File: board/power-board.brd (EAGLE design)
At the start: 95.9 x 90.2 mm, 366 parts, among them J1 H1, J2 H2, J6 DF13-8P-1.25DS, J7 DF13-10P-1.25DS, J8 DF13-4P-1.25DS, J9 DF13-4P-1.25DS, Q1 TPC8120, Q2 TPC8120, Q3 SI7288, U1 INA214DCK, U10 INA214DCK, U11 INA214DCK, U12 INA214DCK, U13 MCP6561T-E/LT, U14 INA214DCK, U15 SN74AUP1G00DCK, U16 SN74LVC1G373DCK, U17 NTHD4508NT1, U18 MCP6561T-E/LT, U19 INA214DCK, U2 INA214DCK, U20 SN74AUP1G00DCK, U21 SN74LVC1G373DCK, U22 NTHD4508NT1, U23 MCP6561T-E/LT, U24 INA214DCK, U25 SN74AUP1G00DCK, U26 SN74LVC1G373DCK, U27 NTHD4508NT1, U28 MCP6561T-E/LT, U29 INA214DCK, U3 INA214DCK, U30 SN74AUP1G00DCK, U31 SN74LVC1G373DCK, U32 NTHD4508NT1, U33 MCP6561T-E/LT, U34 INA214DCK, U35 SN74AUP1G00DCK, U36 SN74LVC1G373DCK, U37 NTHD4508NT1, U38 MCP6561T-E/LT, U39 INA214DCK, U4 INA214DCK, U40 SN74AUP1T08DCK, U41 SN74LVC1G373DCK, U42 FDS8858CZ, U43 TLV3491AIDBV, U44 TPS62132RGT, U45 FDS8858CZ, U46 TLV3491AIDBV, U47 TPS62133RGT, U48 FDS8858CZ, U49 MSP430F2132, U5 INA214DCK, U50 ADG732, U51 SPV1040T, U52 SPV1040T, U53 BQ24650_RVA_16, U54 INA214DCK, U6 INA214DCK, U7 INA214DCK, U8 INA214DCK, U9 INA214DCK, X1 32.768k

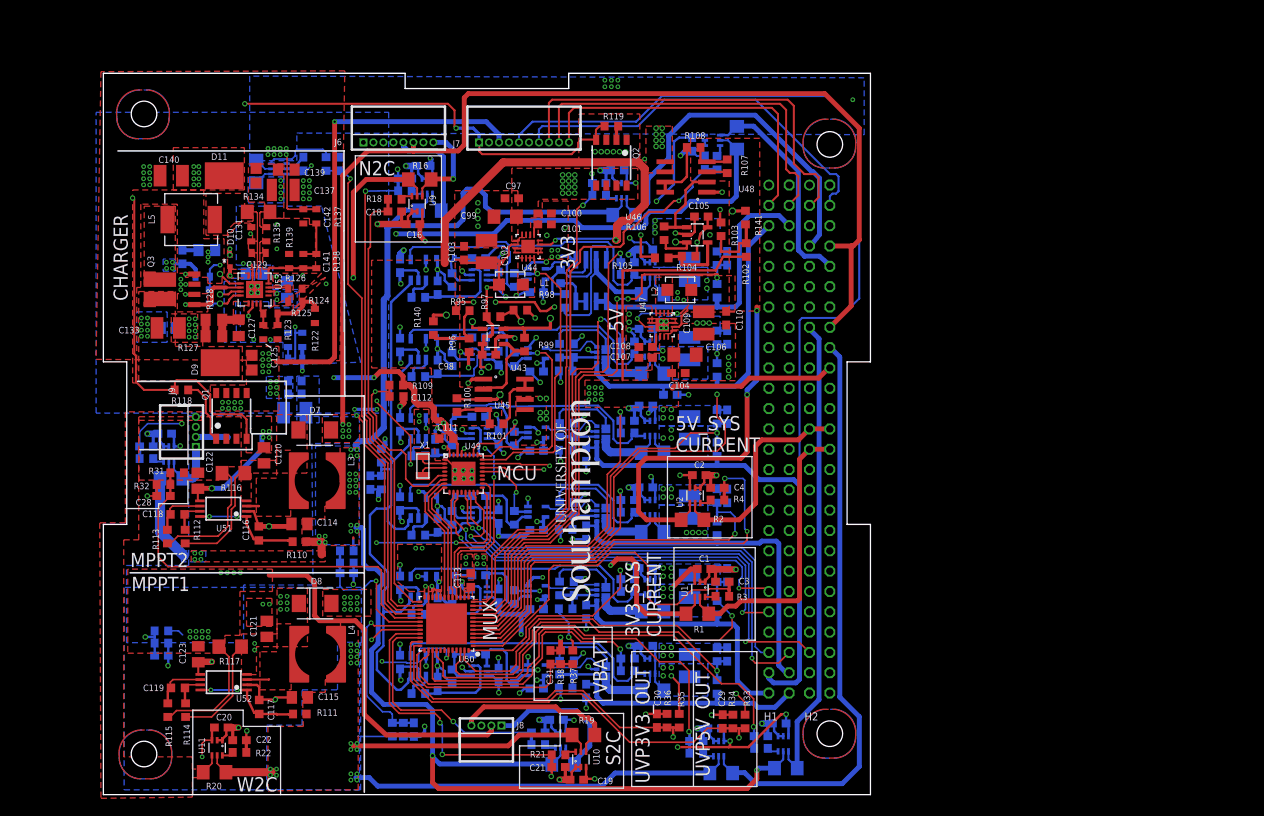
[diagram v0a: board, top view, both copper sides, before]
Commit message: removing deployment switches, adding testpoints
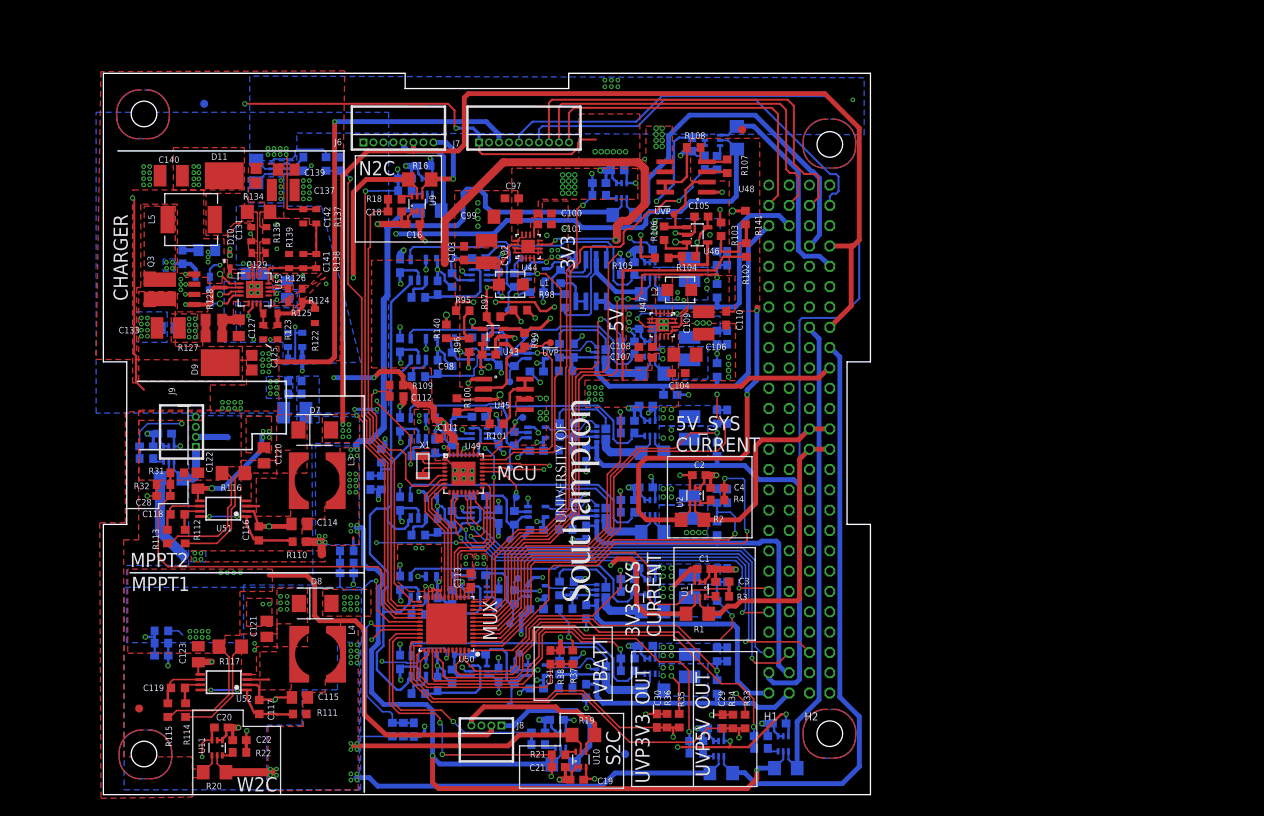
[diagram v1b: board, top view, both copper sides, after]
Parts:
- removed Q1, Q2: TPC8120, gdp_pss_library:SOP8
- removed R118, R119: 1Meg, rcl:R0603
- added FID1, FID2, FID3, FID4: FIDUCIAL1X2-STOP, fiducial:FIDUCIAL-1X2-STOP
- added TP1, TP10, TP11, TP12, TP13, TP14, TP2, TP3, TP4, TP5, TP6, TP7, TP8, TP9: PTR1TP09R, testpad:TP09R
- R39: value 442m -> 50m
- R48: value 43m -> 124m
- moved R140 1.68 mm to (42.9, 57.9)
- moved R99 0.61 mm to (52.6, 56.9)
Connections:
- net 3V3_BU_RADIO renamed 5V_TX_RADIO
- removed net MPPT_BUS: C122.1, Q1.1, Q1.2, Q1.3, R113.1, R116.1, R118.2, R31.2
- removed net REG_VIN: C100.1, C104.1, C106.1, C107.1, C95.1, C97.1, C99.1, J2.20, Q2.5, Q2.6, Q2.7, Q2.8, R102.1, R37.2, R44.2, R53.2, R62.2, R71.2, R80.2, R84.1, R95.1, U39.4, U44.10, U44.11, U44.12, U44.13, U47.10, U47.11, U47.12, U47.13
- new net 5V_RX_RADIO: C53.1, R55.2, U22.1
- net 3V3_RADIO: no longer C53.1, R55.2, U22.1
- net CHARGE_IN: now also C122.1, R113.1, R116.1, R31.2; no longer Q1.5, Q1.6, Q1.7, Q1.8
- net OCP1_COMP_OUT: now also TP12.TP
- net OCP1_MCU_EN: now also TP11.TP
- net OCP1_SENSEM: now also R44.2
- net OCP2_COMP_OUT: now also TP10.TP
- net OCP2_MCU_EN: now also TP9.TP
- net OCP2_SENSEM: now also R53.2
- net OCP3_COMP_OUT: now also TP8.TP
- net OCP3_MCU_EN: now also TP7.TP
- net OCP3_SENSEM: now also R62.2
- net OCP4_COMP_OUT: now also TP6.TP
- net OCP4_MCU_EN: now also TP5.TP
- net OCP4_SENSEM: now also R71.2
- net OCP5_COMP_OUT: now also TP4.TP
- net OCP5_MCU_EN: now also TP3.TP
- net OCP5_SENSEM: now also R80.2
- net OCP6_COMP_OUT: now also TP2.TP
- net OCP6_MCU_EN: now also TP1.TP
- net RBF_A: no longer Q1.4, Q2.4, R118.1, R119.1
- net UVP3V3_GATE: now also TP13.TP
- net UVP3V3_OUT: no longer R39.1, R48.1, U14.4, U19.4
- net UVP5V_GATE: now also TP14.TP
- net UVP5V_OUT: now also R39.1, R48.1, U14.4, U19.4
- net VBATT: now also C100.1, C104.1, C106.1, C107.1, C95.1, C97.1, C99.1, J2.20, R102.1, R37.2, R84.1, R95.1, U39.4, U44.10, U44.11, U44.12, U44.13, U47.10, U47.11, U47.12, U47.13; no longer Q2.1, Q2.2, Q2.3, R119.2
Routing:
- net REG_VIN: track 79.6 -> 0.00 mm, vias 32 -> 0
- net VBATT: track 14.6 -> 86.2 mm, vias 21 -> 49
- net MPPT_BUS: track 24.4 -> 0.00 mm
- net RBF_A: track 121.9 -> 99.8 mm
- net CHARGE_IN: track 65.3 -> 81.5 mm
- net UVP3V3_OUT: track 344.3 -> 337.7 mm
- net GND: track 311.5 -> 305.3 mm
- net UVP3V3_GATE: track 10.9 -> 15.2 mm
- net N$49: track 25.7 -> 22.5 mm
- net OCP6_COMP_OUT: track 14.5 -> 17.8 mm
- net OCP4_COMP_OUT: track 13.5 -> 16.5 mm
- net OCP1_COMP_OUT: track 12.6 -> 15.5 mm
- net OCP2_COMP_OUT: track 10.6 -> 13.3 mm
- net OCP5_MCU_EN: track 26.0 -> 28.6 mm
- net UVP5V_OUT: track 5.67 -> 8.22 mm
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- removed copper zone on layer 1, net MPPT_BUS
- removed copper zone on layer 1, net REG_VIN
- removed copper zone on layer 16, net REG_VIN
- removed copper zone on layer 2, net REG_VIN
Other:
- board text added: "!UVP"
- board text added: "EN"
- board text added: "OCP"

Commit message: done (hopefully)
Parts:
- added TP15, TP16, TP17, TP18, TP19, TP20, TP21, TP22, TP23, TP24, TP25, TP26, TP27, TP28, TP29, TP30: PTR1TP09R, testpad:TP09R
- moved R141 2.01 mm to (78.8, 70.7)
- moved R102 1.55 mm to (78.9, 67.5)
- moved C29 1.22 mm to (76.2, 9.14)
- moved R27 0.81 mm to (35.3, 8.13)
- moved R4 0.73 mm to (77.4, 36.4)
- moved C30 0.61 mm to (68.6, 9.25)
- moved C4 0.61 mm to (77.4, 38.4)
- moved C85 0.61 mm to (78.6, 57.1)
- moved R100 0.61 mm to (44.8, 48.7)
- moved R2 0.61 mm to (74.2, 34.4)
- moved R25 0.61 mm to (30.4, 31.1)
- moved R34 0.61 mm to (78.1, 9.14)
- moved R37 0.61 mm to (59.3, 17.2)
- moved R47 0.61 mm to (76.1, 17.5)
- moved R56 0.61 mm to (76.1, 27.4)
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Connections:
- removed net 3V3_RADIO: J1.51
- net 3V3_FLIGHT_MCU: now also TP24.TP
- net 3V3_SYS: now also TP16.TP
- net 5V_CAMERA: now also TP25.TP
- net 5V_RX_RADIO: now also J1.51, TP26.TP
- net 5V_SYS: now also TP15.TP
- net 5V_TX_RADIO: now also TP27.TP
- net CHARGE_IN: now also TP28.TP
- net GND: now also TP30.TP
- net MPPT2_OUT: now also TP29.TP
- net OCP1_SENSEM: no longer R44.2
- net OCP2_SENSEM: no longer R53.2
- net OCP3_SENSEM: no longer R62.2
- net OCP4_SENSEM: no longer R71.2
- net OCP5_SENSEM: no longer R80.2
- net OEM615_3V3: now also TP23.TP
- net OEM615_LNA_PWR: now also TP22.TP
- net REG3V3: now also TP21.TP
- net REG5V: now also TP20.TP
- net UVP3V3_OUT: now also TP17.TP; no longer C40.1, C51.1
- net UVP5V_OUT: now also C40.1, C51.1, TP18.TP
- net VBATT: now also R44.2, R53.2, R62.2, R71.2, R80.2, TP19.TP
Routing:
- net RBF_A: track 99.8 -> 0.00 mm, vias 3 -> 0
- net 5V_RX_RADIO: track 0.00 -> 35.8 mm
- net 3V3_RADIO: track 33.1 -> 0.00 mm
- net GND: track 305.3 -> 317.1 mm, vias 198 -> 203
- net REG3V3: track 176.0 -> 165.2 mm, vias 8 -> 6
- net UVP3V3_OUT: track 337.7 -> 348.2 mm, vias 69 -> 64
- net CHARGE_IN: track 81.5 -> 89.8 mm, vias 24 -> 26
- net VBATT: track 86.2 -> 94.3 mm, vias 49 -> 45
- net 3V3_SYS: track 36.4 -> 43.4 mm
- net UVP5V_OUT: track 8.22 -> 15.1 mm, vias 15 -> 23
- net N$6: track 8.67 -> 3.18 mm
- net SYS_5V_CSENSE_MUX: track 55.9 -> 51.9 mm
- net 5V_CAMERA: track 44.6 -> 48.3 mm
- net 5V_TX_RADIO: track 30.0 -> 33.8 mm
- net MPPT1_PV_P: track 199.4 -> 195.7 mm
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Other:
- board text added: "!OCP"
- board text added: "0V"
- board text added: "3V3_SYS"
- board text added: "5V_SYS"
- board text added: "CAM"
- board text added: "CHG IN"
- board text added: "GPS"
- board text added: "LNA"
- board text added: "RX"
- board text added: "Rev 1.1 Mar'17"
- board text added: "S/N"
- board text added: "TX"
- board text added: "UVP 3V3"
- board text added: "UVP 5V"
- board text removed: "H1"
- board text removed: "H2"
- board text removed: "OCP"
- board text removed: "Rev 1.1 Dec'16"
- board text removed: "UVP3V3_OUT"
- board text removed: "UVP5V_OUT"

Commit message: committing WIP
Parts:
- added C143, C148, C153, C158: 1u, rcl:C0603K
- added C144, C149, C154, C159: 100n, rcl:C0603K
- added C145, C146, C150, C151, C155, C156, C160, C161: 10u, rcl:C0805K
- added C147, C152, C157, C162: 4.7u, rcl:C0805K
- added D12, D13, D14, D15: 5V1, diode:SMBJ
- added L6, L7, L8, L9: 10uH, gdp_pss_library:MSS7341
- added R118, R119, R143, R144, R145, R147, R148, R149, R151, R152, R153, R155: 1k, rcl:R0603
- added R142, R146, R150, R154: 10m, rcl:R1206
- added TP31, TP32, TP33, TP34, TP35, TP36: PTR1TP09R, testpad:TP09R
- added U55, U56, U57, U58: SPV1040T, gdp_pss_library:TSSOP8
- moved C28 100.9 mm to (108.3, 32.1)
- moved R31 100.9 mm to (110.0, 35.0)
- moved R32 100.9 mm to (108.3, 33.5)
- moved C20 95.6 mm to (101.1, 49.4)
- moved C22 95.6 mm to (103.4, 47.9)
- moved R20 95.6 mm to (100.3, 43.9)
- moved R22 95.6 mm to (103.4, 46.3)
- moved U11 95.6 mm to (100.6, 46.9)
- moved TP29 93.9 mm to (107.3, 25.0)
- moved TP28 93.1 mm to (104.0, 22.1)
- moved TP30 91.7 mm to (107.5, 23.0)
- moved R111 42.2 mm to (14.1, 51.0), turned to 90 degrees
- moved C117 40.2 mm to (16.1, 51.0), turned to 270 degrees
- moved C115 39.7 mm to (22.1, 51.8)
- moved R115 39.7 mm to (11.0, 50.1), turned to 180 degrees
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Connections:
- net MPPT2_OUT renamed MPPT1_MID
- new net MPPT1H_PV_P: C114.1, L3.1, R110.1
- new net MPPT1L_PV_P: C115.1, L4.1, R111.1
- new net MPPT2H_PV_P: C146.1, L6.1, R143.1
- new net MPPT2L_PV_P: C151.1, L7.1, R147.1
- new net MPPT2_MID: C144.2, C145.2, C146.2, C147.2, C150.1, D12.A, R145.1, R146.1, TP32.TP, U55.2, U55.5
- new net MPPT3H_PV_P: C156.1, L8.1, R151.1
- new net MPPT3L_PV_P: C161.1, L9.1, R155.1
- new net MPPT3_MID: C154.2, C155.2, C156.2, C157.2, C160.1, D14.A, R153.1, R154.1, TP35.TP, U57.2, U57.5
- new net N$778: C144.1, R143.2, U55.1, U55.8
- new net N$779: L6.2, U55.3
- new net N$780: C148.1, R144.2, U56.7
- new net N$781: C148.2, R145.2, U56.6
- new net N$782: C152.1, D13.C, R144.1, R146.2, U56.4
- new net N$783: C149.1, R147.2, U56.1, U56.8
- new net N$784: L7.2, U56.3
- new net N$785: C153.1, R148.2, U57.7
- new net N$786: C153.2, R149.2, U57.6
- new net N$787: C157.1, D14.C, R148.1, R150.2, U57.4
- new net N$788: C154.1, R151.2, U57.1, U57.8
- new net N$789: L8.2, U57.3
- new net N$790: C158.1, R152.2, U58.7
- new net N$791: C158.2, R153.2, U58.6
- new net N$792: C162.1, D15.C, R152.1, R154.2, U58.4
- new net N$793: C159.1, R155.2, U58.1, U58.8
- new net N$794: L9.2, U58.3
- new net N$89: C143.1, R118.2, U55.7
- new net N$91: C143.2, R119.2, U55.6
- new net N$92: C147.1, D12.C, R118.1, R142.2, U55.4
- net CHARGE_IN: now also C145.1, C155.1, R119.1, R142.1, R149.1, R150.1, TP31.TP, TP34.TP
- net GND: now also C149.2, C150.2, C151.2, C152.2, C159.2, C160.2, C161.2, C162.2, D13.A, D15.A, TP33.TP, TP36.TP, U56.2, U56.5, U58.2, U58.5
- net MPPT1_PV_P: no longer C114.1, L3.1, R110.1
- net MPPT2_PV_P: no longer C115.1, L4.1, R111.1
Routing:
- net MPPT1_MID: track 224.8 -> 170.6 mm, vias 30 -> 0
- net MPPT_BUS_VSENSE: track 49.5 -> 10.4 mm
- net MSP-TEST: track 59.0 -> 28.1 mm, vias 3 -> 1
- net MPPT2_PV_P: track 222.6 -> 194.8 mm, vias 22 -> 2
- net UVP3V3_OUT: track 348.2 -> 367.2 mm, vias 64 -> 60
- net PV_WEST1_P: track 7.92 -> 25.4 mm
- net N$681: track 8.82 -> 23.9 mm
- net CHARGE_CSENSE_MUX: track 63.0 -> 77.4 mm
- net N$758: track 2.01 -> 15.4 mm
- net N$763: track 14.4 -> 27.2 mm
- net GND: track 317.1 -> 329.4 mm, vias 203 -> 166
- net MPPSET: track 15.9 -> 27.5 mm, vias 2 -> 1
- net N$286: track 14.2 -> 3.30 mm, vias 2 -> 0
- net N$761: track 10.7 -> 0.00 mm
- net N$283: track 14.2 -> 3.57 mm, vias 8 -> 0
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- removed copper zone on layer 1, net CHARGE_IN
- removed copper zone on layer 1, net CHARGE_OUT
- removed copper zone on layer 1, net MPPT1_MID
- removed copper zone on layer 2, net MPPT1_MID
- removed copper zone on layer 1, net MPPT1_PV_P
- removed copper zone on layer 1, net MPPT2_PV_P
- removed copper zone on layer 1, net N$283
- removed copper zone on layer 2, net N$283
- removed copper zone on layer 1, net N$287
- removed copper zone on layer 1, net N$41
- removed copper zone on layer 1, net N$45
- removed copper zone on layer 1, net N$759
- removed copper zone on layer 1, net N$760
- removed copper zone on layer 1, net N$761
- removed copper zone on layer 1, net N$763
- removed copper zone on layer 1, net N$772
- removed copper zone on layer 1, net N$773
- removed copper zone on layer 1, net PROP
- removed copper zone on layer 1, net PV_WEST2_P
- removed copper zone on layer 1, net VREF
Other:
- outline, holes or cut-outs redrawn

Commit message: various bits of routing over a period of time
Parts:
- moved R22 83.0 mm to (31.1, 5.49), flipped to the bottom
- moved C22 82.9 mm to (31.1, 7.32), flipped to the bottom
- moved C20 78.1 mm to (34.1, 9.14), flipped to the bottom
- moved U11 78.0 mm to (34.1, 6.10), flipped to the bottom
- moved R20 77.7 mm to (34.1, 3.05), flipped to the bottom
- moved U6 49.8 mm to (42.1, 6.10)
- moved C10 49.8 mm to (42.1, 9.14)
- moved R10 49.6 mm to (42.1, 3.05)
- moved R12 49.5 mm to (39.0, 5.49)
- moved C12 49.4 mm to (39.0, 7.32)
- moved R153 43.5 mm to (10.4, 50.6)
- moved C160 43.1 mm to (9.75, 53.0)
- moved R150 42.5 mm to (6.71, 59.1), turned to 270 degrees
- moved R155 42.5 mm to (14.6, 52.4), turned to 0 degrees
- moved R151 42.5 mm to (14.6, 62.2), turned to 0 degrees
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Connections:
- net MPPT1H_PV_P: now also R6.2, R9.2, U4.5, U5.5
- net MPPT1L_PV_P: now also R16.2, R19.2, U10.5, U9.5
- net MPPT1_MID: no longer J2.16, J2.8, J9.P$2
- net MPPT1_PV_P: no longer R10.2, R13.2, R5.2, R6.2, R9.2, U3.5, U4.5, U5.5, U6.5, U7.5
- net MPPT2H_PV_P: now also R10.2, R13.2, U6.5, U7.5
- net MPPT2L_PV_P: now also R20.2, R23.2, U11.5, U12.5
- net MPPT2_MID: now also J2.16, J9.P$2
- net MPPT2_PV_P: no longer R15.2, R16.2, R19.2, R20.2, R23.2, U10.5, U11.5, U12.5, U8.5, U9.5
- net MPPT3H_PV_P: now also R5.2, U3.5
- net MPPT3L_PV_P: now also R15.2, U8.5
- net MPPT3_MID: now also J2.8
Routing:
- net MPPT2_PV_P: track 194.8 -> 0.00 mm, vias 2 -> 0
- net MPPT1_PV_P: track 191.6 -> 2.13 mm, vias 2 -> 0
- net MPPT2_MID: track 4.07 -> 188.6 mm, vias 0 -> 14
- net MPPT3L_PV_P: track 5.37 -> 116.0 mm, vias 0 -> 4
- net MPPT2H_PV_P: track 5.17 -> 92.7 mm, vias 0 -> 3
- net MPPT1H_PV_P: track 5.02 -> 77.6 mm, vias 0 -> 3
- net MPPT2L_PV_P: track 5.17 -> 77.0 mm, vias 0 -> 1
- net MPPT1L_PV_P: track 5.87 -> 75.3 mm, vias 0 -> 3
- net MPPT1_MID: track 170.6 -> 107.6 mm, vias 0 -> 1
- net MPPT3H_PV_P: track 5.37 -> 67.9 mm
- net PV_WEST2_P: track 0.00 -> 49.7 mm
- net GND: track 329.4 -> 373.0 mm, vias 166 -> 140
- net UVP3V3_OUT: track 367.2 -> 334.2 mm, vias 60 -> 58
- net N$92: track 3.49 -> 28.6 mm, vias 0 -> 2
- net N$283: track 3.57 -> 28.3 mm, vias 0 -> 2
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- added copper zone on layer 15, net MPPT1_MID
- added copper zone on layer 15, net MPPT2_MID
- removed copper zone on layer 16, net CHARGE_IN
- removed copper zone on layer 2, net CHARGE_IN
- removed copper zone on layer 16, net CHARGE_OUT
- removed copper zone on layer 2, net GND
- removed copper zone on layer 16, net MPPT1_MID
- removed copper zone on layer 16, net MPPT1_PV_P
- removed copper zone on layer 16, net MPPT2_PV_P
- removed copper zone on layer 16, net N$757
- removed copper zone on layer 16, net N$760
- removed copper zone on layer 16, net N$763
- removed copper zone on layer 2, net N$763
- removed copper zone on layer 16, net N$775
- removed copper zone on layer 2, net N$776
- removed copper zone on layer 2, net N$777
- removed copper zone on layer 16, net PROP
- removed copper zone on layer 2, net PROP
- removed copper zone on layer 16, net VREF

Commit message: some routing
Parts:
- moved R31 80.1 mm to (30.5, 25.6), flipped to the bottom
- moved C28 78.5 mm to (30.5, 21.9), flipped to the bottom
- moved R32 78.4 mm to (30.5, 23.8), flipped to the bottom
- moved C27 30.4 mm to (30.5, 36.6)
- moved C124 29.1 mm to (5.08, 70.0), turned to 90 degrees
- moved R30 28.1 mm to (30.5, 34.7)
- moved R29 26.2 mm to (30.5, 32.9), turned to 0 degrees
- moved R121 24.2 mm to (4.37, 66.0), turned to 270 degrees
- moved R120 24.0 mm to (5.99, 66.0), turned to 270 degrees
- moved C134 15.6 mm to (4.70, 73.6), flipped to the top
- moved R129 13.2 mm to (20.7, 67.1), flipped to the top, turned to 270 degrees
- moved C128 10.5 mm to (22.6, 67.1), flipped to the top
- moved R132 8.31 mm to (21.8, 85.8), turned to 180 degrees
- moved R6 8.00 mm to (34.1, 77.4), flipped to the top, turned to 180 degrees
- moved C8 7.91 mm to (30.5, 73.8), flipped to the top, turned to 90 degrees
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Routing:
- net MPPT3_MID: track 22.2 -> 147.3 mm, vias 0 -> 24
- net GND: track 373.0 -> 486.5 mm, vias 140 -> 253
- net CHARGE_IN: track 95.7 -> 191.8 mm, vias 0 -> 8
- net PROP: track 15.5 -> 97.8 mm, vias 0 -> 9
- net MPPT1L_PV_P: track 75.3 -> 154.9 mm, vias 3 -> 8
- net MPPT1H_PV_P: track 77.6 -> 144.2 mm, vias 3 -> 9
- net MPPT1_MID: track 107.6 -> 168.4 mm, vias 1 -> 29
- net MSP-TEST: track 28.1 -> 71.6 mm
- net CHARGE_OUT: track 3.36 -> 38.8 mm, vias 0 -> 9
- net UVP3V3_OUT: track 334.2 -> 309.0 mm, vias 58 -> 59
- net PV_WEST1_CSENSE_MUX: track 49.7 -> 25.6 mm
- net VBATT: track 83.1 -> 106.7 mm, vias 37 -> 45
- net N$761: track 0.07 -> 14.6 mm
- net MPPT2H_PV_P: track 92.7 -> 106.2 mm, vias 3 -> 5
- net MPPT3L_PV_P: track 116.0 -> 103.4 mm, vias 4 -> 3
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- added copper zone on layer 1, net MPPT1_MID
- added copper zone on layer 1, net MPPT3_MID
- added copper zone on layer 15, net MPPT3_MID
- removed copper zone on layer 15, net N$774
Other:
- board text removed: "N2C"

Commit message: some more routing
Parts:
- moved SH2 19.0 mm to (3.07, 79.1)
- moved TP21 2.51 mm to (60.8, 69.9)
- moved R109 0.42 mm to (39.0, 51.8)
- moved C112 0.34 mm to (39.0, 50.0)
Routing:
- net UVP3V3_OUT: track 309.0 -> 283.1 mm, vias 59 -> 57
- net PV_WEST1_P: track 44.6 -> 68.1 mm, vias 0 -> 5
- net PV_WEST2_P: track 49.7 -> 64.1 mm, vias 0 -> 2
- net N$782: track 26.1 -> 38.8 mm, vias 1 -> 5
- net CHARGE_IN: track 191.8 -> 202.6 mm
- net MSP-RST: track 64.7 -> 73.1 mm
- net GND: track 486.5 -> 494.0 mm, vias 253 -> 256
- net MPPT1_MID: track 168.4 -> 174.3 mm
- net MPPT2L_PV_P: track 89.4 -> 93.7 mm, vias 1 -> 6
- net MSP-TEST: track 71.6 -> 67.3 mm
- net MPPT1L_PV_P: track 154.9 -> 153.0 mm
- net MPPT2H_PV_P: track 106.2 -> 108.1 mm
- net MPPT2_MID: track 194.5 -> 196.0 mm, vias 18 -> 21
- net CHARGE_CSENSE_MUX: track 68.6 -> 69.9 mm
- net PV_NORTH1_CSENSE_MUX: track 56.5 -> 57.7 mm
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- added copper zone on layer 1, net MPPT3L_PV_P

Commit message: changing mppt voltage monitoring points
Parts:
- removed C27: 1u, rcl:C0603
- removed R29: 309k, rcl:R0603
- removed R30: 100k, rcl:R0603
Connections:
- net MPPT1_PV_VSENSE renamed MPPT2_LOWER_PV_VSENSE
- net MPPT2_PV_VSENSE renamed MPPT2_MID_PV_VSENSE
- removed net MPPT1_PV_P: R25.2
- removed net MPPT2_OUT_VSENSE: C27.1, R29.1, R30.2
- removed net MPPT2_PV_P: R27.2
- net GND: no longer C27.2, R30.1
- net MPPT1_MID: no longer R29.2
- net MPPT2L_PV_P: now also R25.2, R27.2
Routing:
- net MPPT1_MID: track 174.3 -> 165.2 mm, vias 29 -> 28
- net GND: track 494.0 -> 498.7 mm, vias 256 -> 255
- net MPPT2_OUT_VSENSE: track 4.36 -> 0.00 mm
- net MUX_OUT: track 48.5 -> 49.4 mm
